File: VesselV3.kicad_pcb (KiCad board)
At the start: 2 copper layers, 341.8 x 195.5 mm, 396 parts, among them IC1 USB3320C-EZK-TR, IC3 5VOutput_VoltageRegulator, IC4 BidirectionalLogicLevelShifter, IC6 AND Gate, J1 JTAG/SWD 10pins Headers, Y1 25MHz

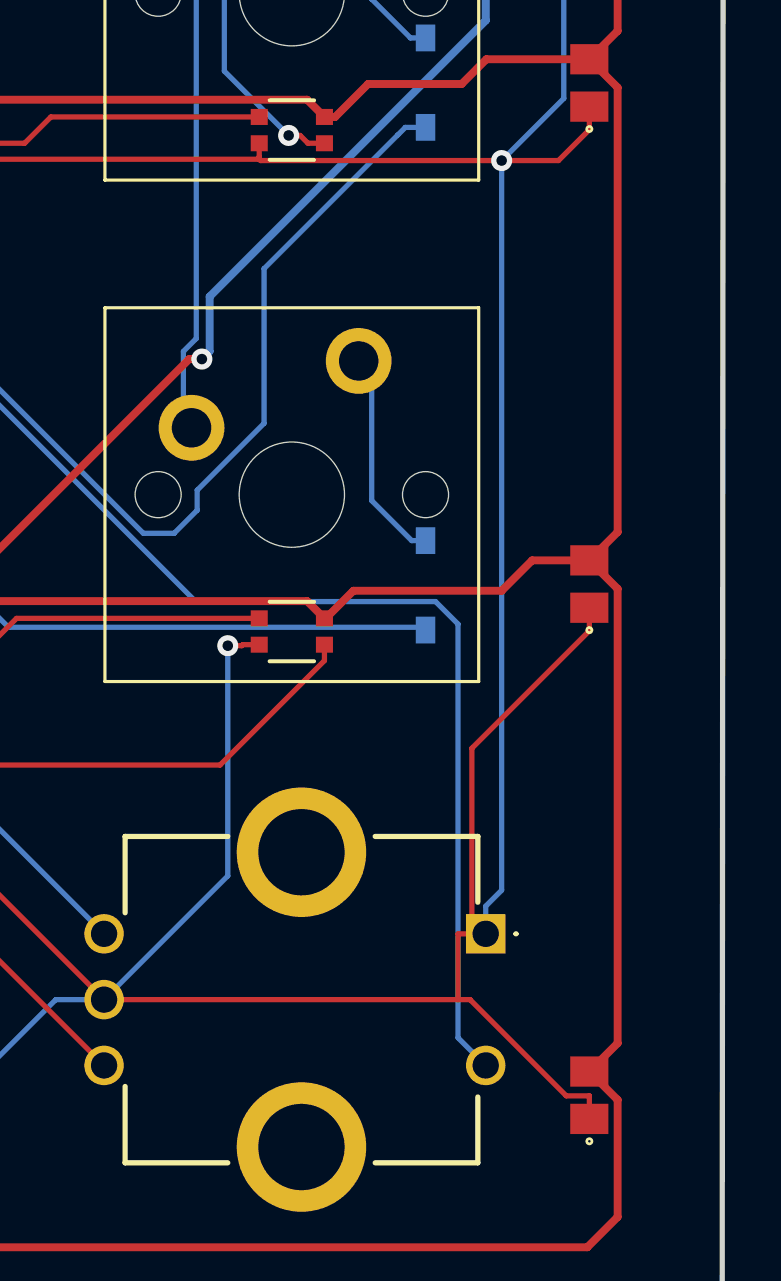
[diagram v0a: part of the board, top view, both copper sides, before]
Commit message: Encoder Push - Pull-up and DRC
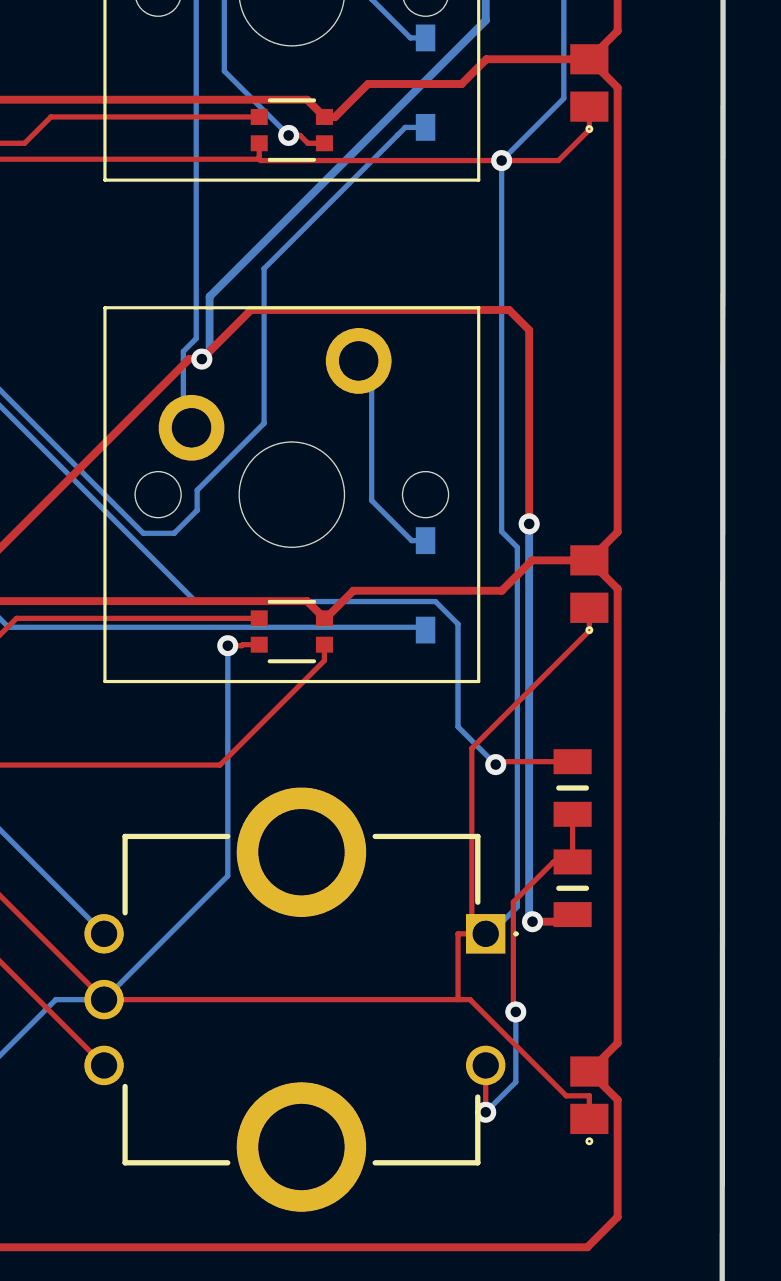
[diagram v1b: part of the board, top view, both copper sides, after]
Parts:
- added R21: 10k, SamacSys_Parts:RESC2012X50N, F.Cu at (377.7, 199.3)
- added R22: 10k, SamacSys_Parts:RESC2012X50N, F.Cu at (377.7, 203.1)
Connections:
- S4 pad 2: ROTARY-ENC_PUSH -> Net-(S4-NO)
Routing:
- net +5V: track 410.2 -> 447.9 mm, vias 7 -> 9
- net Net-(S4-NO): track 0.00 -> 15.0 mm, vias 0 -> 2
- net ROTARY-ENC_PUSH: track 264.8 -> 256.5 mm, vias 1 -> 2
- net GND: track 3407.2 -> 3407.8 mm

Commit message: Improved routing
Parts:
- moved R1 0.38 mm to (338.3, 33.6)
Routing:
- net COL5: track 210.4 -> 195.3 mm, vias 1 -> 2
- net Net-(USB-C1-VBUS_1): track 22.1 -> 23.6 mm
- net Net-(D4-A): track 9.23 -> 7.88 mm
- net Net-(D28-A): track 9.23 -> 7.89 mm
- net Net-(D2-A): track 9.24 -> 7.91 mm
- net Net-(D47-A): track 9.24 -> 7.91 mm
- net Net-(D63-A): track 9.21 -> 8.05 mm
- net Net-(D8-A): track 8.95 -> 8.05 mm
- net GND: track 3407.8 -> 3407.0 mm
